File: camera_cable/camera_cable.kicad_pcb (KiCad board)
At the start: 4 copper layers, 42.2 x 63.7 mm, 2 parts

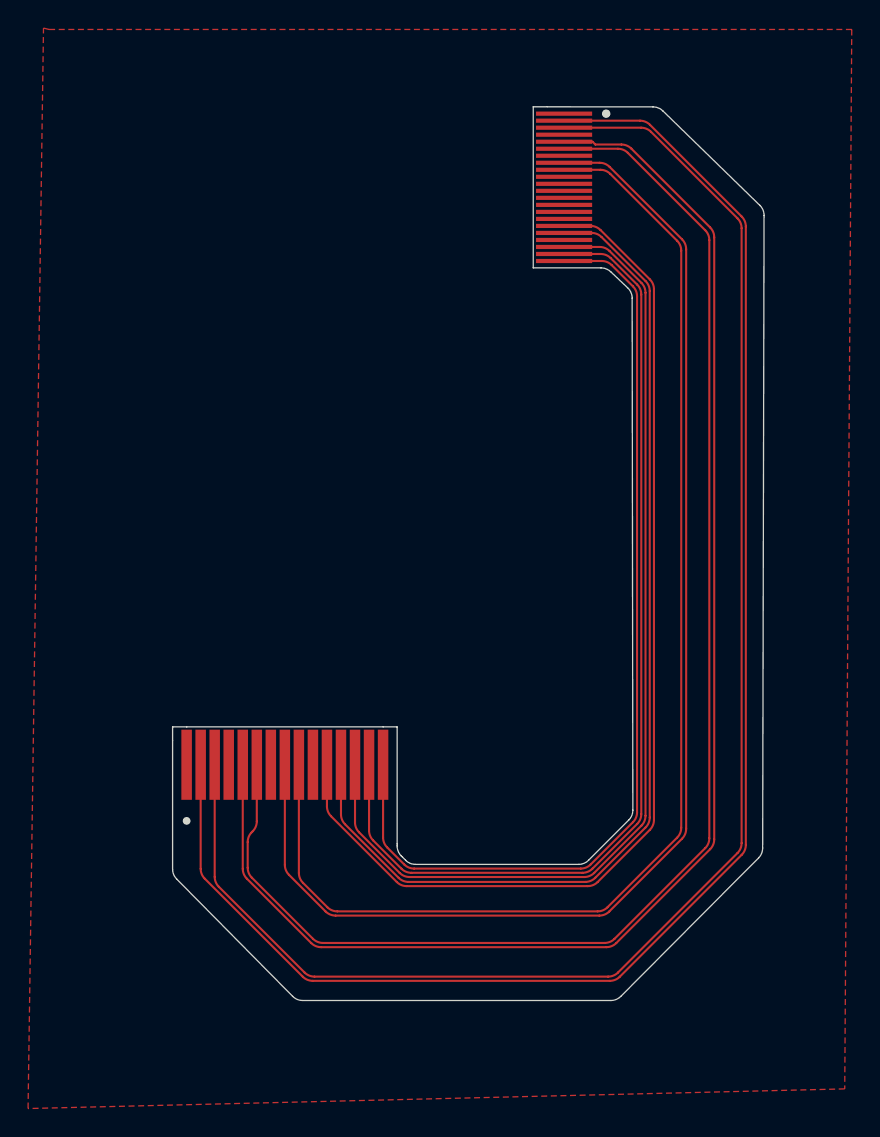
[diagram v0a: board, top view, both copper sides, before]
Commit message: 2 layer fpc with vias
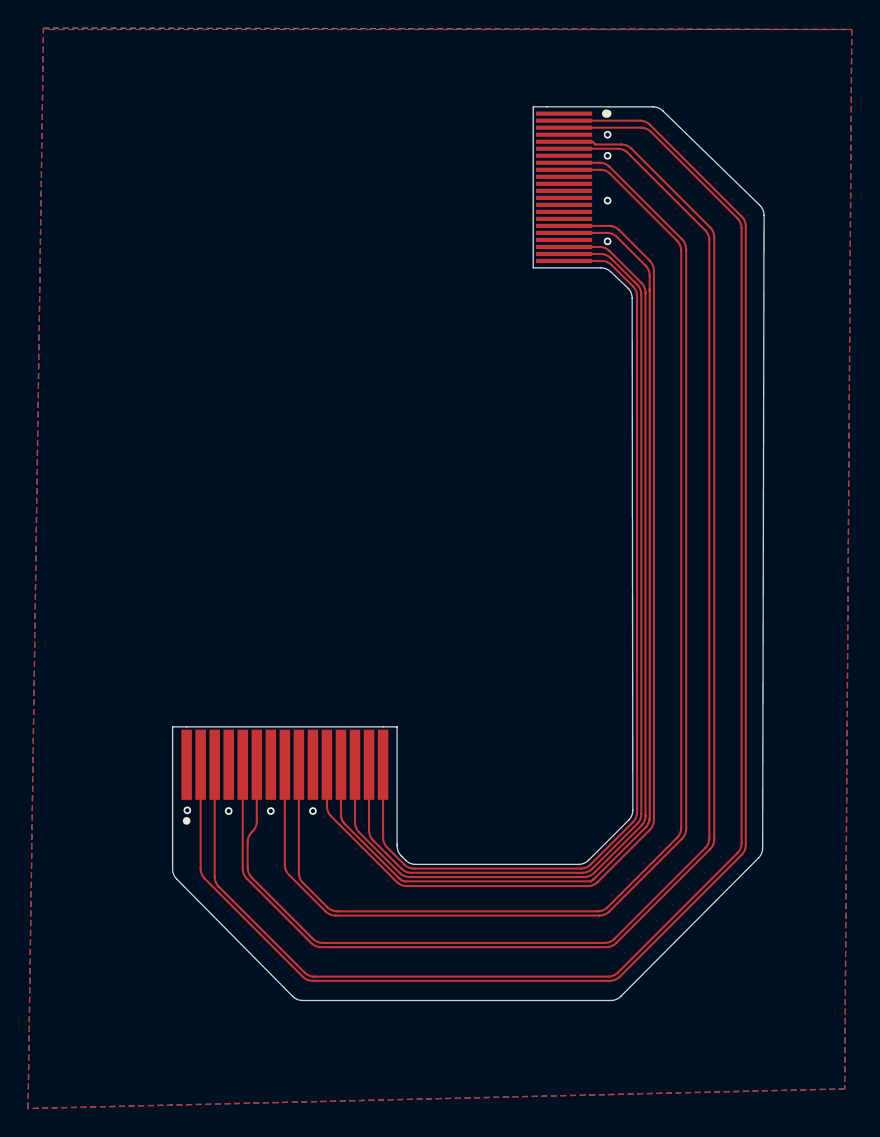
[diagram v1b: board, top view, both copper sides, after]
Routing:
- net Net-(J2-CAM_IO0): track 77.1 -> 77.9 mm
- net Net-(J2-CAM_IO1): track 75.2 -> 75.9 mm
- net GND: vias 0 -> 9
- added copper zone on B.Cu, net GND
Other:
- board text added: "STIFFENER: 0.25 mm PI"
- board text removed: "STIFFENER: 0.2 mm FR4"

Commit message: fixed and reordered
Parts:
- turned J2 to 90 degrees
- turned j1 to 180 degrees
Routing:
- net Net-(J2-CAM_3v3): track 69.5 -> 118.3 mm
- net Net-(J2-CAM_SDA): track 71.2 -> 116.4 mm
- net Net-(J2-CAM_SCA): track 73.3 -> 114.6 mm
- net Net-(J2-CAM_D0_N): track 114.2 -> 75.5 mm
- net Net-(J2-CAM_D0_P): track 112.3 -> 77.6 mm
- net Net-(J2-CAM_IO1): track 75.9 -> 106.4 mm
- net Net-(J2-CAM_IO0): track 77.9 -> 104.5 mm
- net Net-(J2-CAM_D1_N): track 103.4 -> 85.7 mm
- net Net-(J2-CAM_D1_P): track 101.8 -> 87.5 mm
- net Net-(J2-CAM_CK_P): track 90.9 -> 95.6 mm
- net Net-(J2-CAM_CK_N): track 92.8 -> 93.8 mm
- net GND: track 0.00 -> 0.14 mm, vias 9 -> 10
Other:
- board size 42.2 x 63.7 mm -> 42.1 x 63.9 mm
- board text added: "STIFFENER: 0.2 mm PI"
- board text removed: "STIFFENER: 0.25 mm PI"
